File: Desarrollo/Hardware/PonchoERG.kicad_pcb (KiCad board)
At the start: 2 copper layers, 86.4 x 80.5 mm, 96 parts, among them J1 Entradas Analógicas, J2 I/O's Multi Propósito, U1 TPD2E001, U10 ADS1299, U11 ADuM6401, U12 ADuM2401, U13 NCP1117ST33T3G, U14 OPA2376_NI, U15 TPD2E001, U2 TPD2E001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

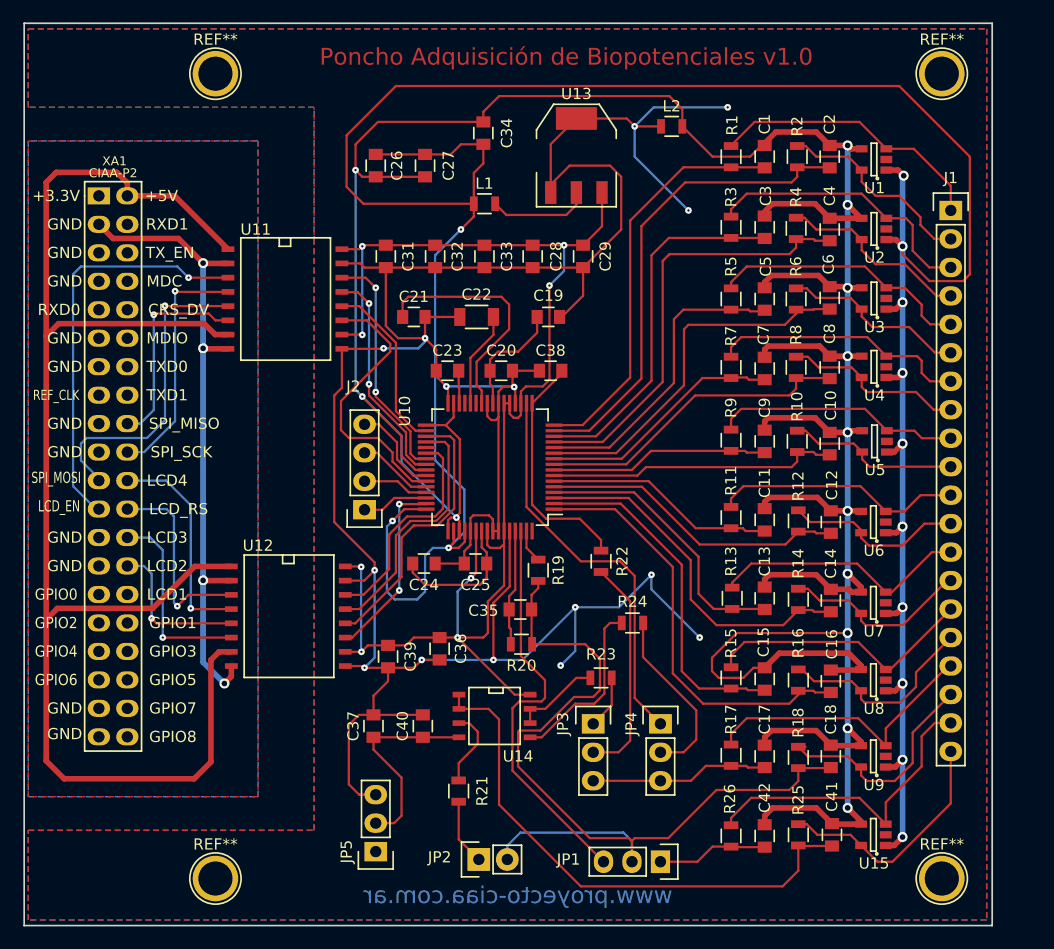
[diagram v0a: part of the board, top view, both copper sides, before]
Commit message: Actualización de esquemático, se completaron campos de "Hoja de dato" y "Código Digikey" para cada componente. Se completaron los rótulos de hojas. Versión Final de PCB. Actualización de tamaño de pistas y redimensión de zonas de relleno. Lista de Materiales actualizada en carpeta "Documentación".
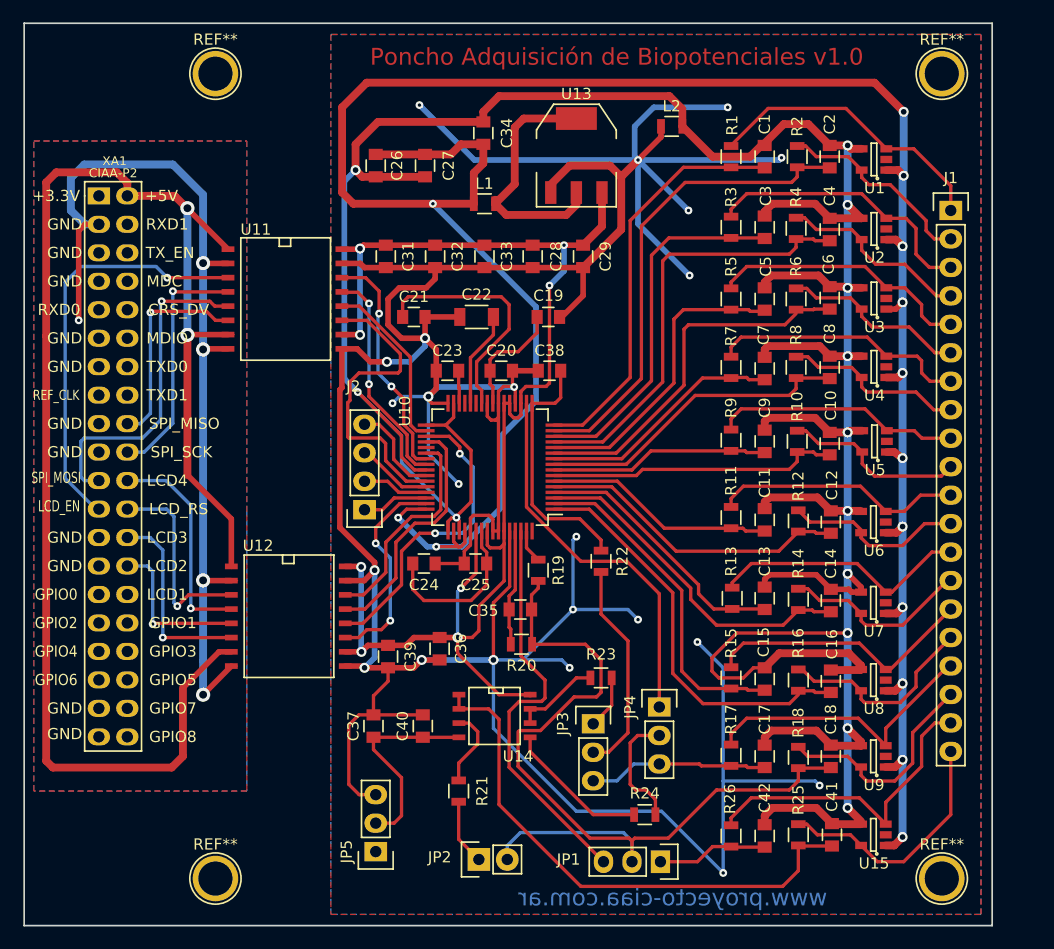
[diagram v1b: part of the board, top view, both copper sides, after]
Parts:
- C36, C37: value NI -> 1uF
- C38: value NI -> 1nF
- JP5: value -AVSS -> AVSS(-)
- R21: value NI -> 10k
- U14: value OPA2376_NI -> OPA2376
- moved R24 17.1 mm to (156.5, 125.1)
- moved JP4 1.50 mm to (157.8, 115.5)
- moved C38 0.10 mm to (148.0, 85.5), turned to 180 degrees
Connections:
- C38 pad 1: GNDA -> Net-(C38-Pad1)
- C38 pad 2: Net-(C38-Pad2) -> GNDA
- R22 pad 2: Net-(C38-Pad2) -> Net-(C38-Pad1)
- U10 pad 17: Net-(C38-Pad2) -> Net-(C38-Pad1)
- U13 pad 4: GNDA -> Net-(L1-Pad2)
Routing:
- net GNDA: track 257.3 -> 372.6 mm, vias 15 -> 23
- net /AISLACIÓN/GND_NISO: track 59.5 -> 86.2 mm, vias 4 -> 5
- net +3V3: track 244.6 -> 221.4 mm, vias 13 -> 14
- net Net-(C38-Pad1): track 0.00 -> 22.6 mm
- net Net-(C38-Pad2): track 21.5 -> 0.00 mm
- net Net-(L1-Pad2): track 9.14 -> 22.8 mm
- net Net-(JP4-Pad2): track 16.0 -> 10.7 mm
- net Net-(R24-Pad2): track 15.8 -> 12.9 mm
- net Earth: track 300.8 -> 303.6 mm
- net /ADS1299/PWDN/: track 25.2 -> 27.9 mm, vias 0 -> 2
- net /ADS1299/MISO: track 24.7 -> 27.4 mm
- net Net-(C24-Pad1): track 12.5 -> 14.9 mm
- net /ADS1299/DRDY/: track 16.8 -> 19.0 mm
- net /ADS1299/IN7-: track 32.1 -> 30.6 mm
- net /ADS1299/IN7+: track 25.1 -> 23.6 mm
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
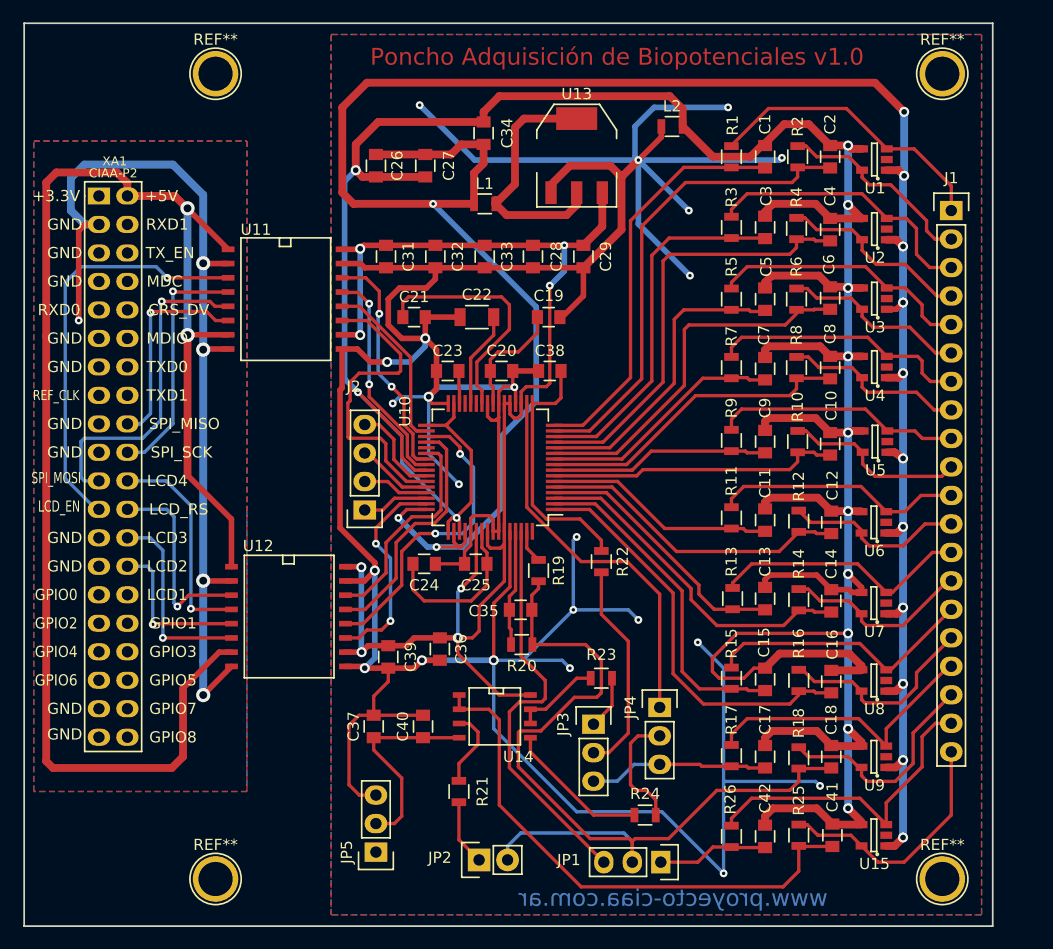
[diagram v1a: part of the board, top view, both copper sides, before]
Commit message: Revisión del SCH. Eliminación de JP5. Revisión de PCB y modificación de pistas basada en correción de errores del DRC. Se eliminaron todos los errores manteniendo el diseño. REVISAR. Además se quitaron las zonas de cobre debajo de los ADuM.
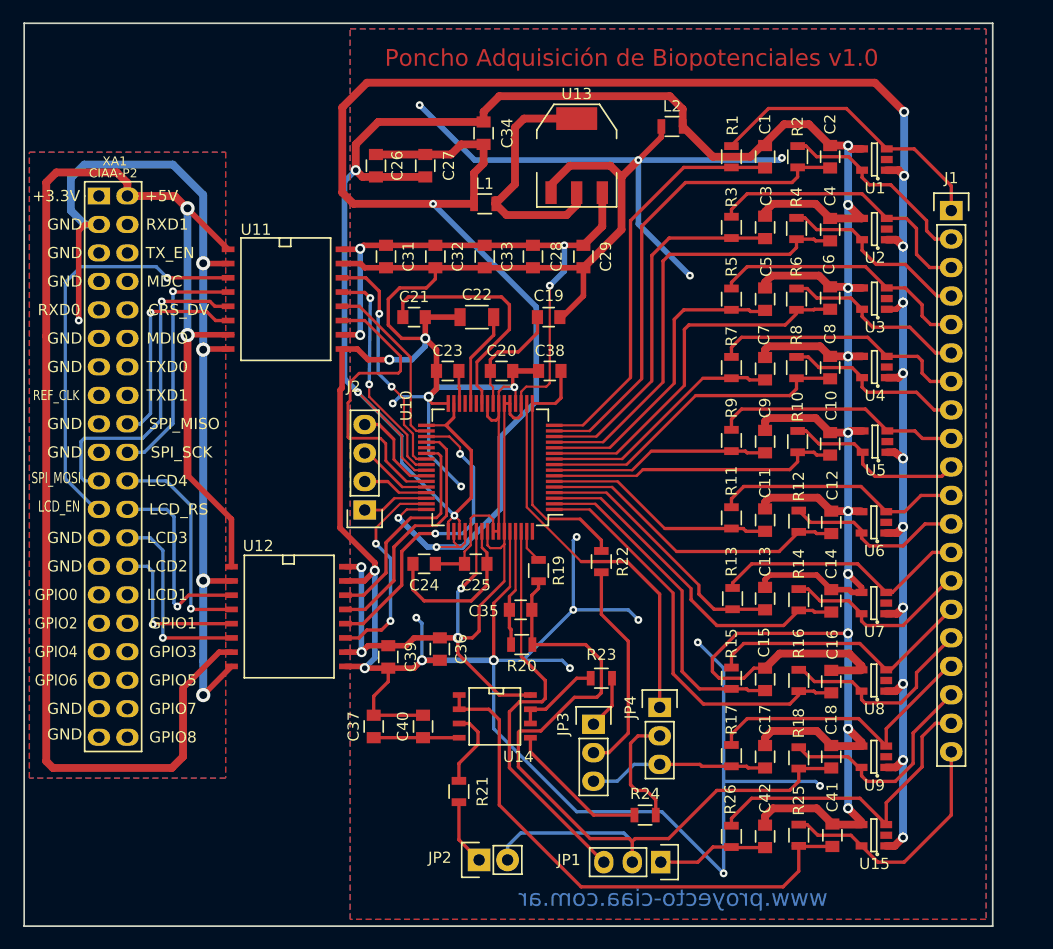
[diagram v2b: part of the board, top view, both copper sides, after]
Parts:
- removed JP5: AVSS(-), Pin_Headers:Pin_Header_Straight_1x03
- removed REF** (x4): 1pin, Connect:1pin
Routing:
- net GNDA: track 372.6 -> 347.6 mm, vias 23 -> 22
- net Net-(C37-Pad1): track 18.2 -> 7.63 mm
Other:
- net class Default: clearance 0.1 -> 0.2
- rule trace_clearance: 0.1 -> 0.2

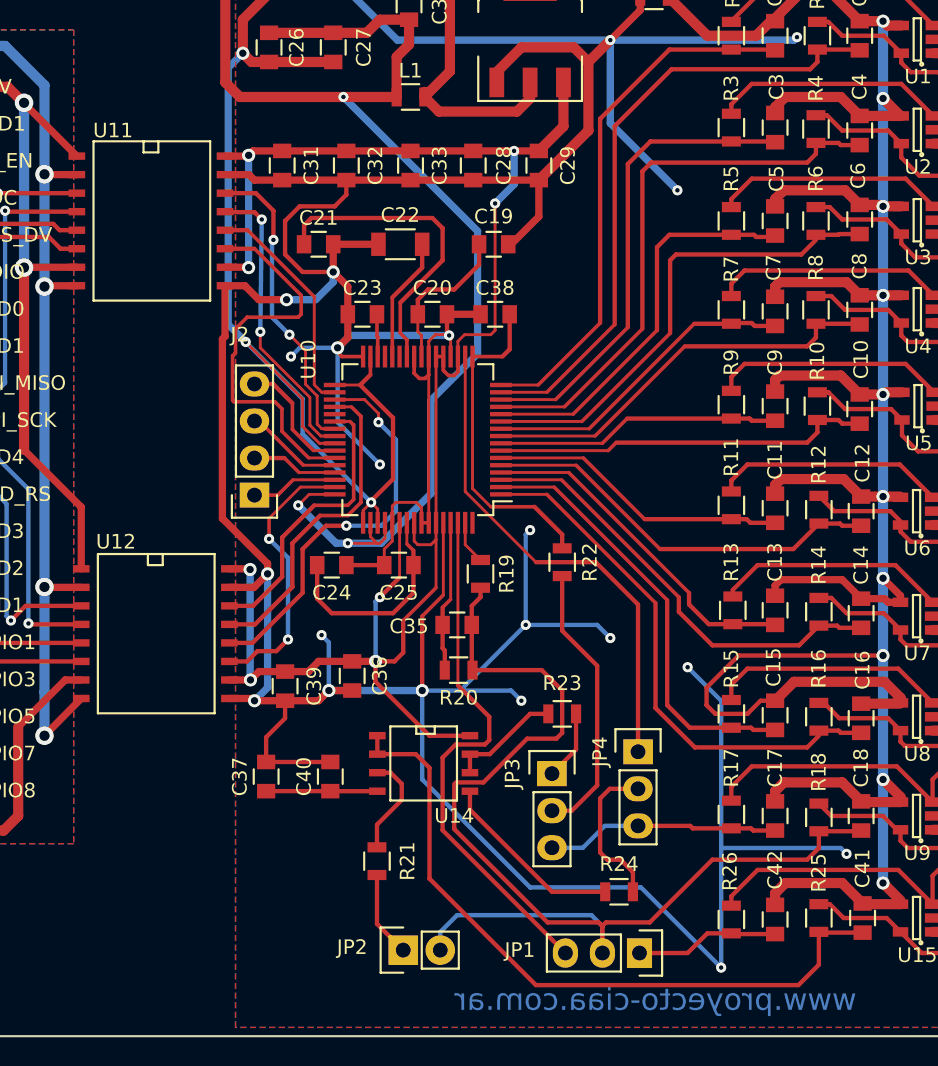
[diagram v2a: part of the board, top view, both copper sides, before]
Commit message: Actualización final. Se añadieron dimensiones, referencias para ubicación correcta de ICs. Se añadieron vías nuevas entre planos top y bottom de masa (GNDA). REALIZAR REVISIÓN FINAL.
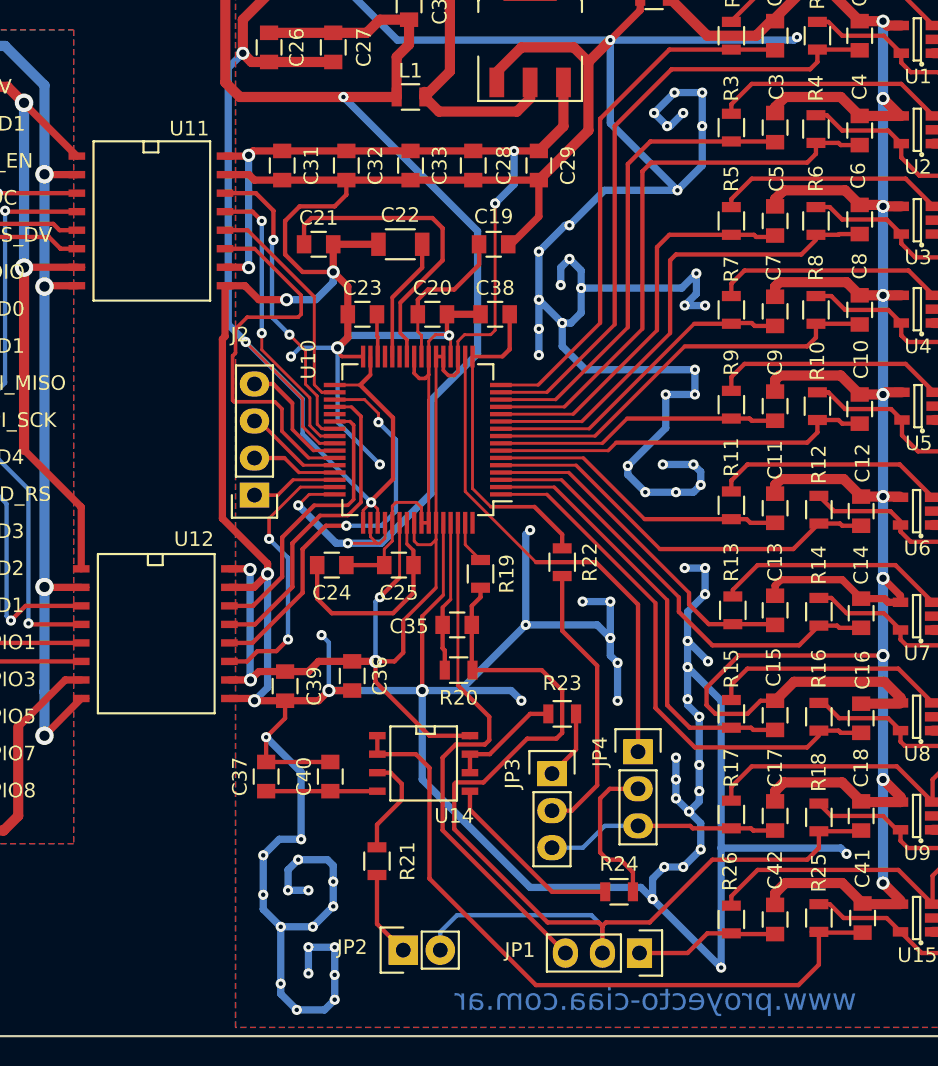
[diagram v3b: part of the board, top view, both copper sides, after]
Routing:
- net GNDA: track 347.6 -> 521.8 mm, vias 22 -> 88
- net /ADS1299/SCLK: track 21.1 -> 20.2 mm
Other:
- board text removed: "Borrar (Footprint MP1) la Plantilla-EDU-CIAA al finalizar el posicionamiento y definido el borde de PCB."
- board text removed: "Diseño simple faz. Sin requerimientos especiales."
- board text removed: "Editar el rótulo"
- board text removed: "Editar el stackup para reflejar cantidad de capas, si se han realizado cálculos de impedancia o si es relevante para el funcionamiento."
- board text removed: "Para un diseño nuevo luego de modificar el esquemático: 1)Seleccionar el bloque del PCB y cotas. (click-drag-release). 2)Opción de borrar bloque (Botón derecho). 3)Marcar todo menos locked footprints (MP1 y XA1) 4) Aceptar. 5) Volver a cargar el netlist."
- board text removed: "STACK-UP"
- board text removed: "Se sugiere colocar código de Poncho en cobre, serigrafía y rótulo."
